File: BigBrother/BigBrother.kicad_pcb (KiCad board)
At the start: 2 copper layers, 4 parts, among them J1 RPi_GPIO, U1 bno055, U2 BMP388, U3 VHN5019_Breakout

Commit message: Board!! maybe done!!!
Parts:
- moved U1 4.15 mm to (145.0, 56.0)
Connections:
- J1 pad 1: Net-(J1-Pad1) -> 3.3V
- J1 pad 14: Net-(J1-Pad14) -> GND
- J1 pad 20: GND2 -> GND
- J1 pad 25: Net-(J1-Pad25) -> GND
- J1 pad 30: Net-(J1-Pad30) -> GND
- J1 pad 34: Net-(J1-Pad34) -> GND
- J1 pad 39: Net-(J1-Pad39) -> GND
- J1 pad 6: Net-(J1-Pad6) -> GND
- U3 pad 8: GND2 -> GND
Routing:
- net GPIO_INA: track 0.00 -> 40.0 mm
- net GPIO_INB: track 0.00 -> 24.4 mm
- net SCL: track 0.00 -> 8.62 mm
- net 3.3V: track 0.00 -> 7.70 mm
- net SDA: track 0.00 -> 7.57 mm
- net GPIO_PWM: track 0.00 -> 6.67 mm
- net TXD: track 0.00 -> 5.24 mm
- net RXD: track 0.00 -> 5.24 mm
- added copper zone on F.Cu, net 3.3V
- added copper zone on B.Cu, net GND
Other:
- board outline added: 67 x 71 mm

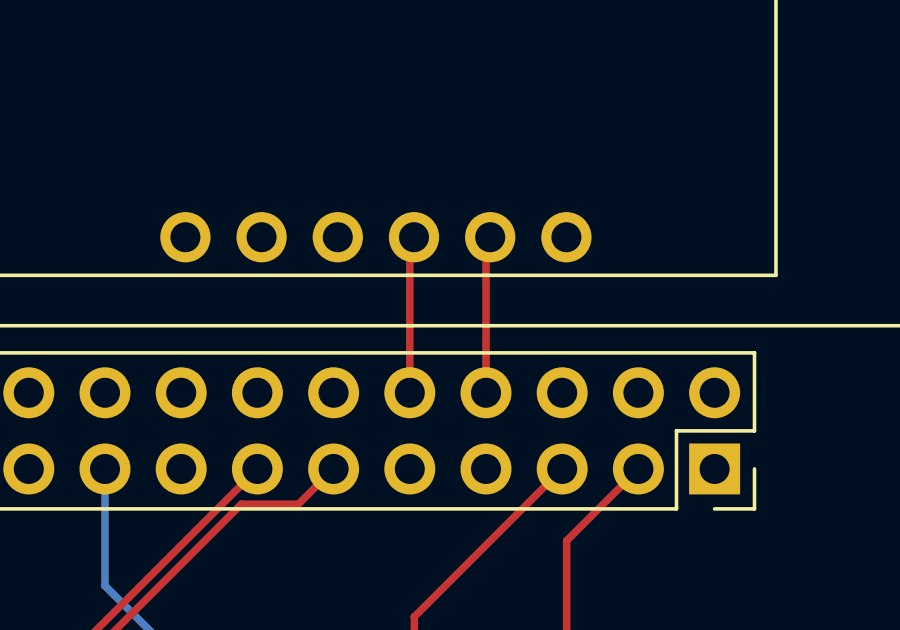
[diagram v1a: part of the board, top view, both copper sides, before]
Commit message: I forgot RST
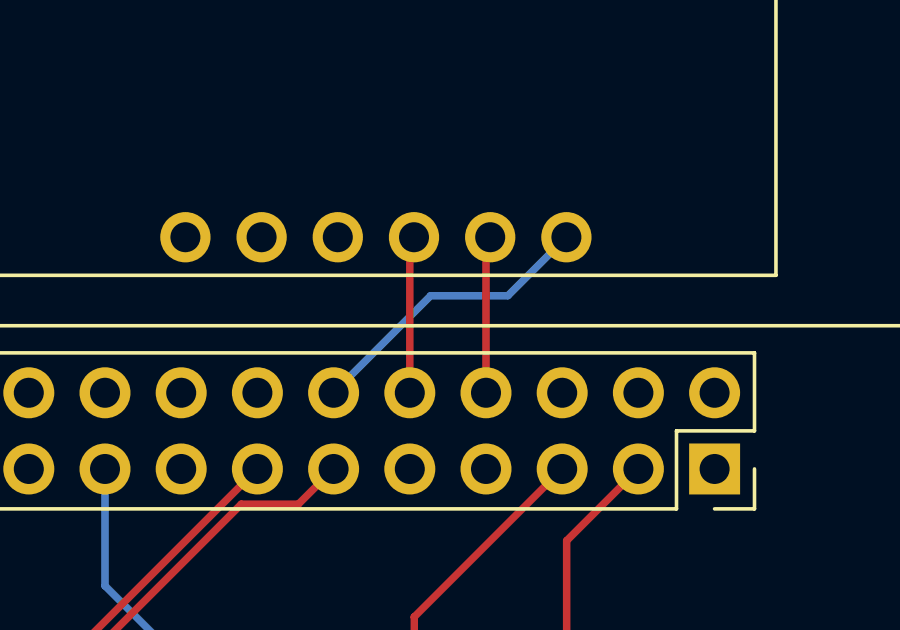
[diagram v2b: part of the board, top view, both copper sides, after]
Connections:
- J1 pad 12: Net-(J1-Pad12) -> RST
- U1 pad 6: Net-(U1-Pad6) -> RST
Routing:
- net RST: track 0.00 -> 9.91 mm
